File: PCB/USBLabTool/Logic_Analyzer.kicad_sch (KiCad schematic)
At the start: 20 parts, among them U18 74HC245N, U19 74HC245N

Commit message: minor fixes
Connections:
- net +3V3 renamed +3.3V
- net LOGIC_OUT0 renamed LOGIC_INP0
- net LOGIC_OUT1 renamed LOGIC_INP1
- net LOGIC_OUT10 renamed LOGIC_INP10
- net LOGIC_OUT11 renamed LOGIC_INP11
- net LOGIC_OUT12 renamed LOGIC_INP12
- net LOGIC_OUT13 renamed LOGIC_INP13
- net LOGIC_OUT14 renamed LOGIC_INP14
- net LOGIC_OUT15 renamed LOGIC_INP15
- net LOGIC_OUT2 renamed LOGIC_INP2
- net LOGIC_OUT3 renamed LOGIC_INP3
- net LOGIC_OUT4 renamed LOGIC_INP4
- net LOGIC_OUT5 renamed LOGIC_INP5
- net LOGIC_OUT6 renamed LOGIC_INP6
- net LOGIC_OUT7 renamed LOGIC_INP7
- net LOGIC_OUT8 renamed LOGIC_INP8
- net LOGIC_OUT9 renamed LOGIC_INP9

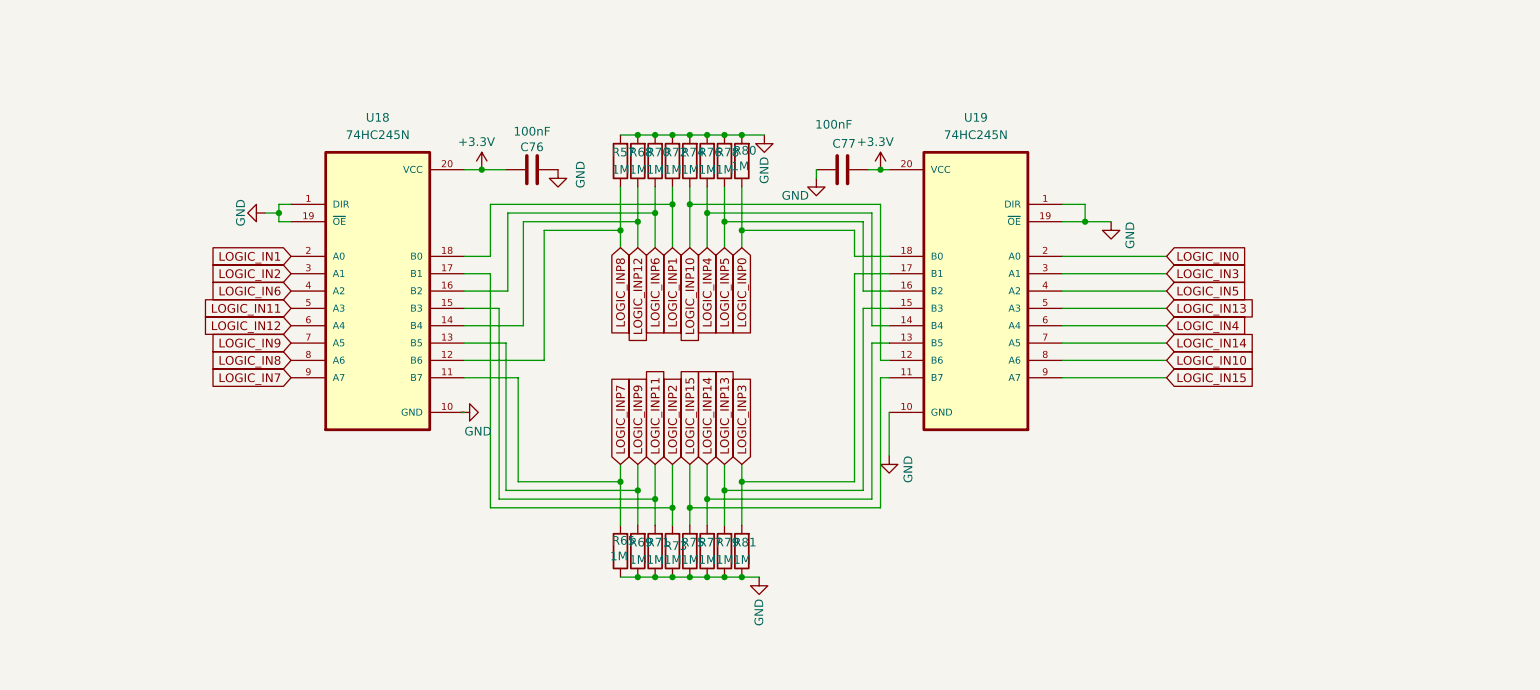
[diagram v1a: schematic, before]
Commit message: rearrange logic pins, connectors, fix some name tags
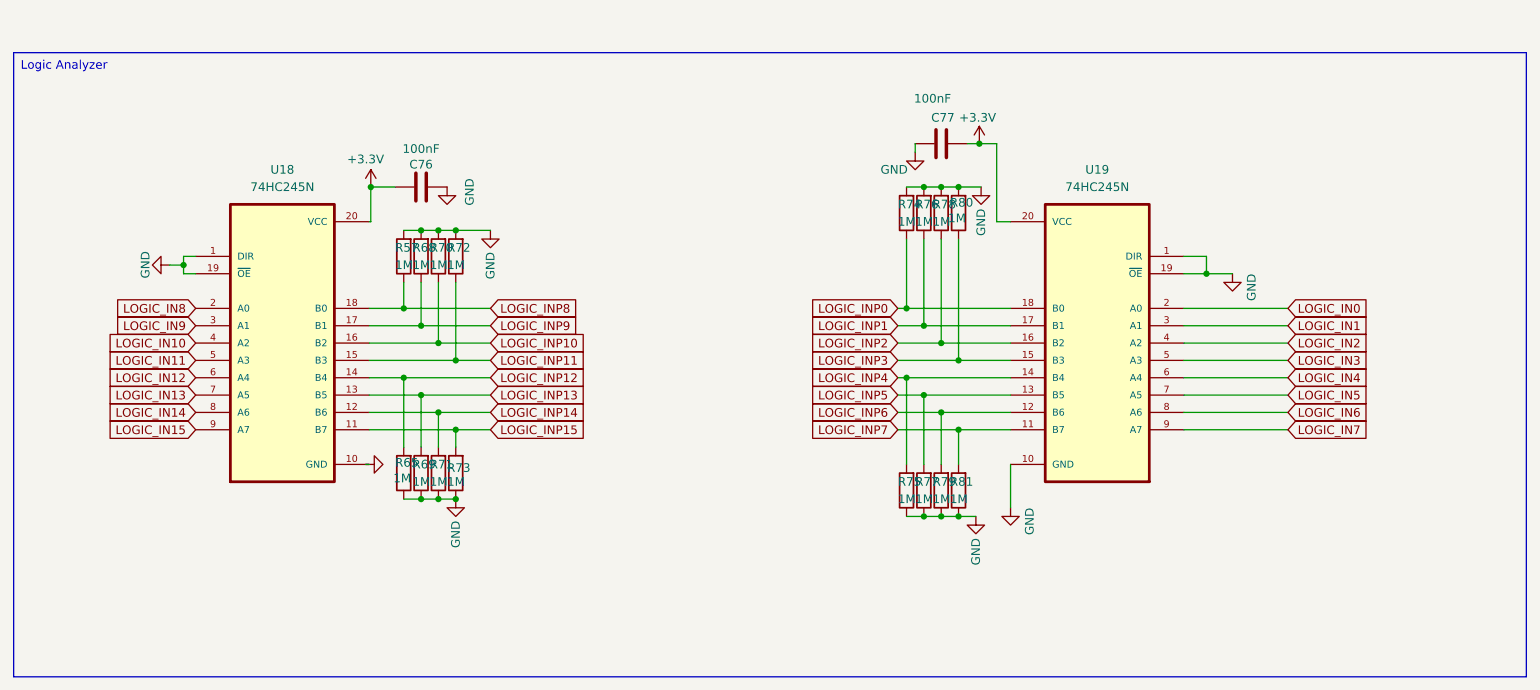
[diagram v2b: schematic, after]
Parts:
- U18: footprint Package_SO:SOIC-20W_7.5x12.8mm_P1.27mm -> Package_DFN_QFN:DHVQFN-20-1EP_2.5x4.5mm_P0.5mm_EP1x3mm
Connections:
- net LOGIC_IN1: now also U19.3 (A1); no longer U18.2 (A0)
- net LOGIC_IN10: now also U18.4 (A2); no longer U19.8 (A6)
- net LOGIC_IN13: now also U18.7 (A5); no longer U19.5 (A3)
- net LOGIC_IN14: now also U18.8 (A6); no longer U19.7 (A5)
- net LOGIC_IN15: now also U18.9 (A7); no longer U19.9 (A7)
- net LOGIC_IN2: now also U19.4 (A2); no longer U18.3 (A1)
- net LOGIC_IN3: now also U19.5 (A3); no longer U19.3 (A1)
- net LOGIC_IN5: now also U19.7 (A5); no longer U19.4 (A2)
- net LOGIC_IN6: now also U19.8 (A6); no longer U18.4 (A2)
- net LOGIC_IN7: now also U19.9 (A7); no longer U18.9 (A7)
- net LOGIC_IN8: now also U18.2 (A0); no longer U18.8 (A6)
- net LOGIC_IN9: now also U18.3 (A1); no longer U18.7 (A5)
- net LOGIC_INP0: now also R74.1; no longer R80.1
- net LOGIC_INP1: now also R76.1, U19.17 (B1); no longer R72.1, U18.18 (B0)
- net LOGIC_INP10: now also R70.1, U18.16 (B2); no longer R74.1, U19.12 (B6)
- net LOGIC_INP11: now also R72.1; no longer R71.2
- net LOGIC_INP12: now also R65.2; no longer R68.1
- net LOGIC_INP13: now also R69.2, U18.13 (B5); no longer R79.2, U19.15 (B3)
- net LOGIC_INP14: now also R71.2, U18.12 (B6); no longer R77.2, U19.13 (B5)
- net LOGIC_INP15: now also R73.2, U18.11 (B7); no longer R75.2, U19.11 (B7)
- net LOGIC_INP2: now also R78.1, U19.16 (B2); no longer R73.2, U18.17 (B1)
- net LOGIC_INP3: now also R80.1, U19.15 (B3); no longer R81.2, U19.17 (B1)
- net LOGIC_INP4: now also R75.2; no longer R76.1
- net LOGIC_INP5: now also R77.2, U19.13 (B5); no longer R78.1, U19.16 (B2)
- net LOGIC_INP6: now also R79.2, U19.12 (B6); no longer R70.1, U18.16 (B2)
- net LOGIC_INP7: now also R81.2, U19.11 (B7); no longer R65.2, U18.11 (B7)
- net LOGIC_INP8: now also U18.18 (B0); no longer U18.12 (B6)
- net LOGIC_INP9: now also R68.1, U18.17 (B1); no longer R69.2, U18.13 (B5)
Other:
- moved on the sheet: C76, C77, R57, R65, R68, R69, R70, R71, R72, R73, R74, R75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

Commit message: Update logic analyzer schematic
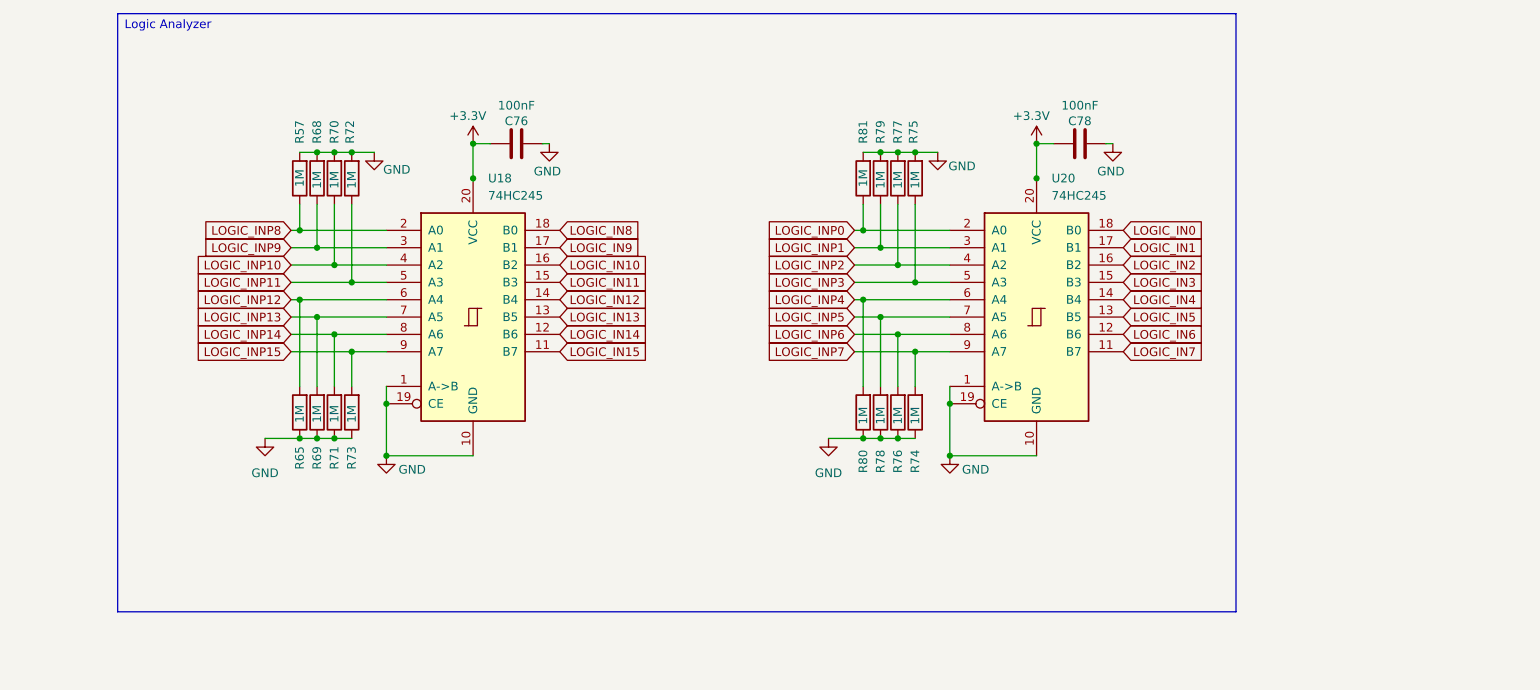
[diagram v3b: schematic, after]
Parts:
- removed C77: 100nF, Capacitor_SMD:C_0603_1608Metric, symbol Device:C
- removed U18: 74HC245N, Package_DFN_QFN:DHVQFN-20-1EP_2.5x4.5mm_P0.5mm_EP1x3mm, symbol 74HC245N(SMD):74HC245N
- removed U19: 74HC245N, Package_SO:SOIC-20W_7.5x12.8mm_P1.27mm, symbol 74HC245N(SMD):74HC245N
- added C78: 100nF, Capacitor_SMD:C_0603_1608Metric, symbol Device:C
- added U18, U20: 74HC245, Package_DFN_QFN:DHVQFN-20-1EP_2.5x4.5mm_P0.5mm_EP1x3mm, symbol 74xx:74HC245
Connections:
- net +3.3V: now also C78.1, U18.20 (VCC), U20.20 (VCC)
- net GND: now also R74.1, R75.2, R76.1, R77.2, R78.1, R79.2, R80.1, R81.2, C78.2, U18.1 (A->B), U18.10 (GND), U18.19 (CE), U20.1 (A->B), U20.10 (GND), U20.19 (CE); no longer R74.2, R75.1, R76.2, R77.1, R78.2, R79.1, R80.2, R81.1
- net LOGIC_IN0: now also U20.18 (B0)
- net LOGIC_IN1: now also U20.17 (B1)
- net LOGIC_IN10: now also U18.16 (B2)
- net LOGIC_IN11: now also U18.15 (B3)
- net LOGIC_IN12: now also U18.14 (B4)
- net LOGIC_IN13: now also U18.13 (B5)
- net LOGIC_IN14: now also U18.12 (B6)
- net LOGIC_IN15: now also U18.11 (B7)
- net LOGIC_IN2: now also U20.16 (B2)
- net LOGIC_IN3: now also U20.15 (B3)
- net LOGIC_IN4: now also U20.14 (B4)
- net LOGIC_IN5: now also U20.13 (B5)
- net LOGIC_IN6: now also U20.12 (B6)
- net LOGIC_IN7: now also U20.11 (B7)
- net LOGIC_IN8: now also U18.18 (B0)
- net LOGIC_IN9: now also U18.17 (B1)
- net LOGIC_INP0: now also R81.1, U20.2 (A0); no longer R74.1
- net LOGIC_INP1: now also R79.1, U20.3 (A1); no longer R76.1
- net LOGIC_INP10: now also U18.4 (A2)
- net LOGIC_INP11: now also U18.5 (A3)
- net LOGIC_INP12: now also U18.6 (A4)
- net LOGIC_INP13: now also U18.7 (A5)
- net LOGIC_INP14: now also U18.8 (A6)
- net LOGIC_INP15: now also U18.9 (A7)
- net LOGIC_INP2: now also R77.1, U20.4 (A2); no longer R78.1
- net LOGIC_INP3: now also R75.1, U20.5 (A3); no longer R80.1
- net LOGIC_INP4: now also R80.2, U20.6 (A4); no longer R75.2
- net LOGIC_INP5: now also R78.2, U20.7 (A5); no longer R77.2
- net LOGIC_INP6: now also R76.2, U20.8 (A6); no longer R79.2
- net LOGIC_INP7: now also R74.2, U20.9 (A7); no longer R81.2
- net LOGIC_INP8: now also U18.2 (A0)
- net LOGIC_INP9: now also U18.3 (A1)
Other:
- note added: "Logic Analyzer"

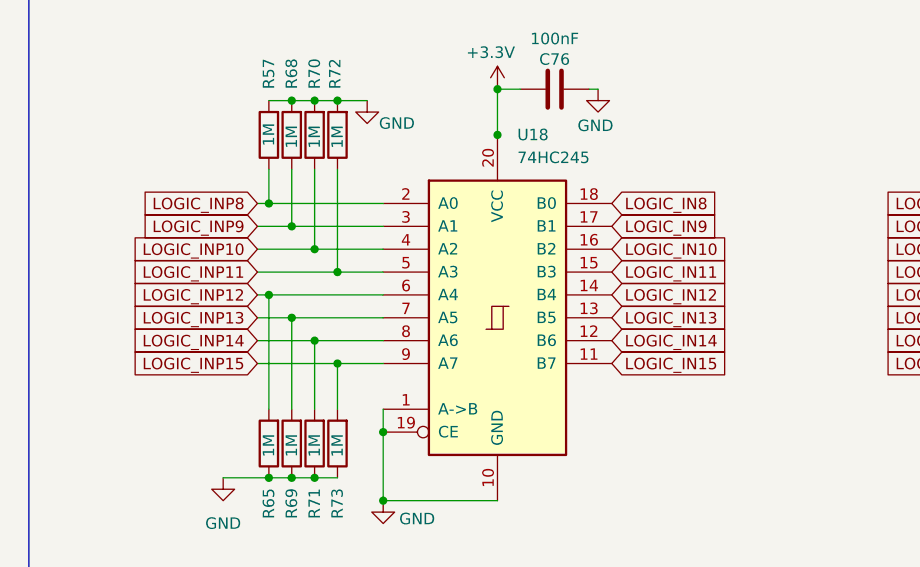
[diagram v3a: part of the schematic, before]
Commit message: Updated schematic and PCB
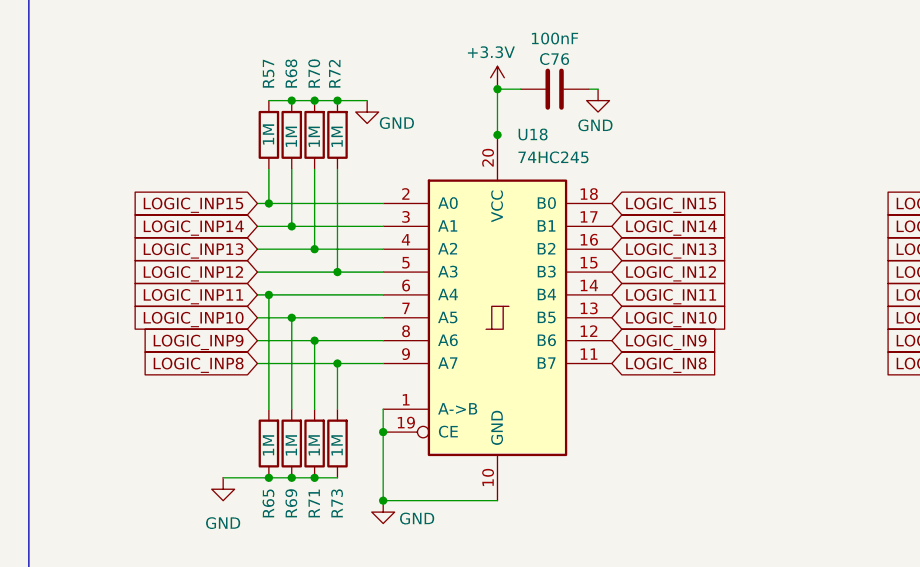
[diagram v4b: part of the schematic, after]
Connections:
- net LOGIC_IN10: now also U18.13 (B5); no longer U18.16 (B2)
- net LOGIC_IN11: now also U18.14 (B4); no longer U18.15 (B3)
- net LOGIC_IN12: now also U18.15 (B3); no longer U18.14 (B4)
- net LOGIC_IN13: now also U18.16 (B2); no longer U18.13 (B5)
- net LOGIC_IN14: now also U18.17 (B1); no longer U18.12 (B6)
- net LOGIC_IN15: now also U18.18 (B0); no longer U18.11 (B7)
- net LOGIC_IN8: now also U18.11 (B7); no longer U18.18 (B0)
- net LOGIC_IN9: now also U18.12 (B6); no longer U18.17 (B1)
- net LOGIC_INP10: now also R69.2, U18.7 (A5); no longer R70.1, U18.4 (A2)
- net LOGIC_INP11: now also R65.2, U18.6 (A4); no longer R72.1, U18.5 (A3)
- net LOGIC_INP12: now also R72.1, U18.5 (A3); no longer R65.2, U18.6 (A4)
- net LOGIC_INP13: now also R70.1, U18.4 (A2); no longer R69.2, U18.7 (A5)
- net LOGIC_INP14: now also R68.1, U18.3 (A1); no longer R71.2, U18.8 (A6)
- net LOGIC_INP15: now also R57.1, U18.2 (A0); no longer R73.2, U18.9 (A7)
- net LOGIC_INP8: now also R73.2, U18.9 (A7); no longer R57.1, U18.2 (A0)
- net LOGIC_INP9: now also R71.2, U18.8 (A6); no longer R68.1, U18.3 (A1)

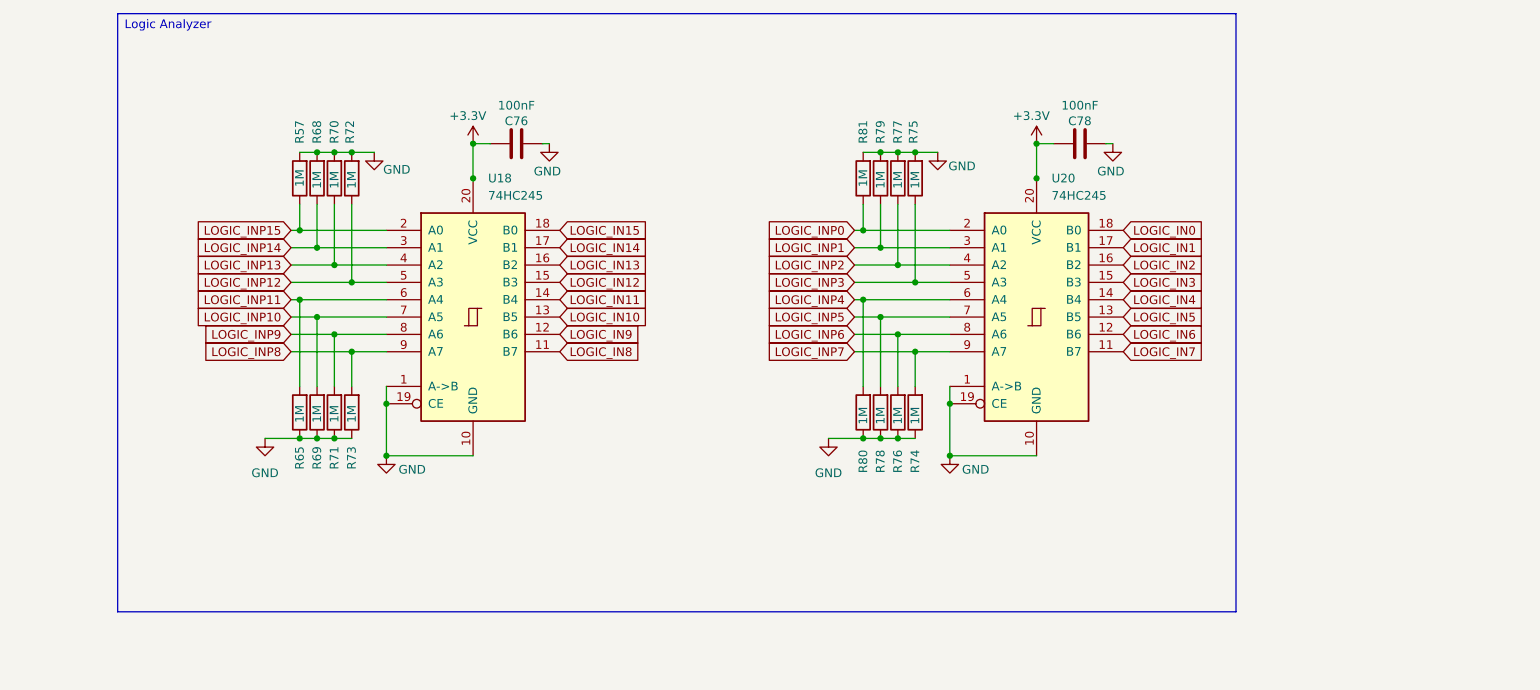
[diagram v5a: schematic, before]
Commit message: Resolved DRC/ERC errors in PCB and schematic
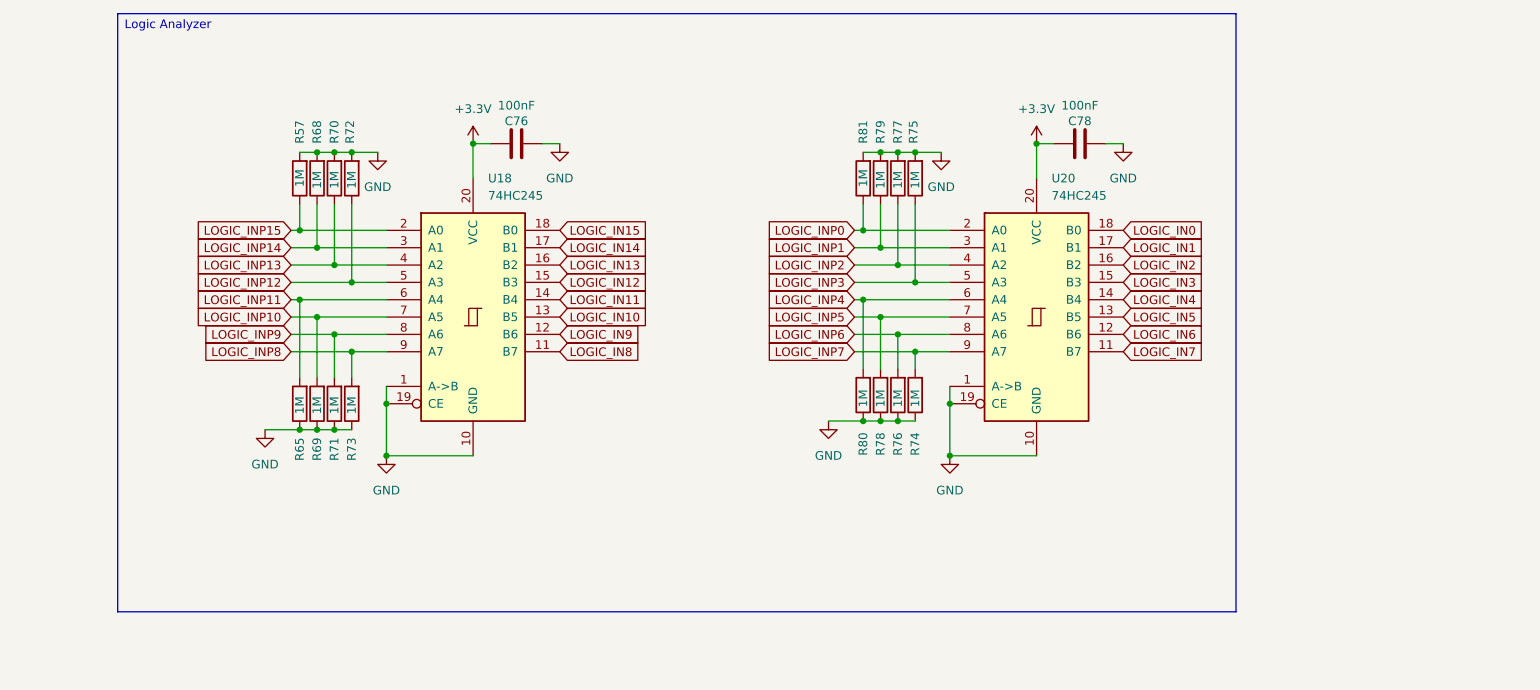
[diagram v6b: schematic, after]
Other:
- moved on the sheet: R65, R69, R71, R73, R74, R76, R78, R80
